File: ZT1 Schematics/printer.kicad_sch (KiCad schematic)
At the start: 5 parts, among them P103 Conn_02x20_Odd_Even, U101 74LS74, U102 74LS373, U103 74LS02

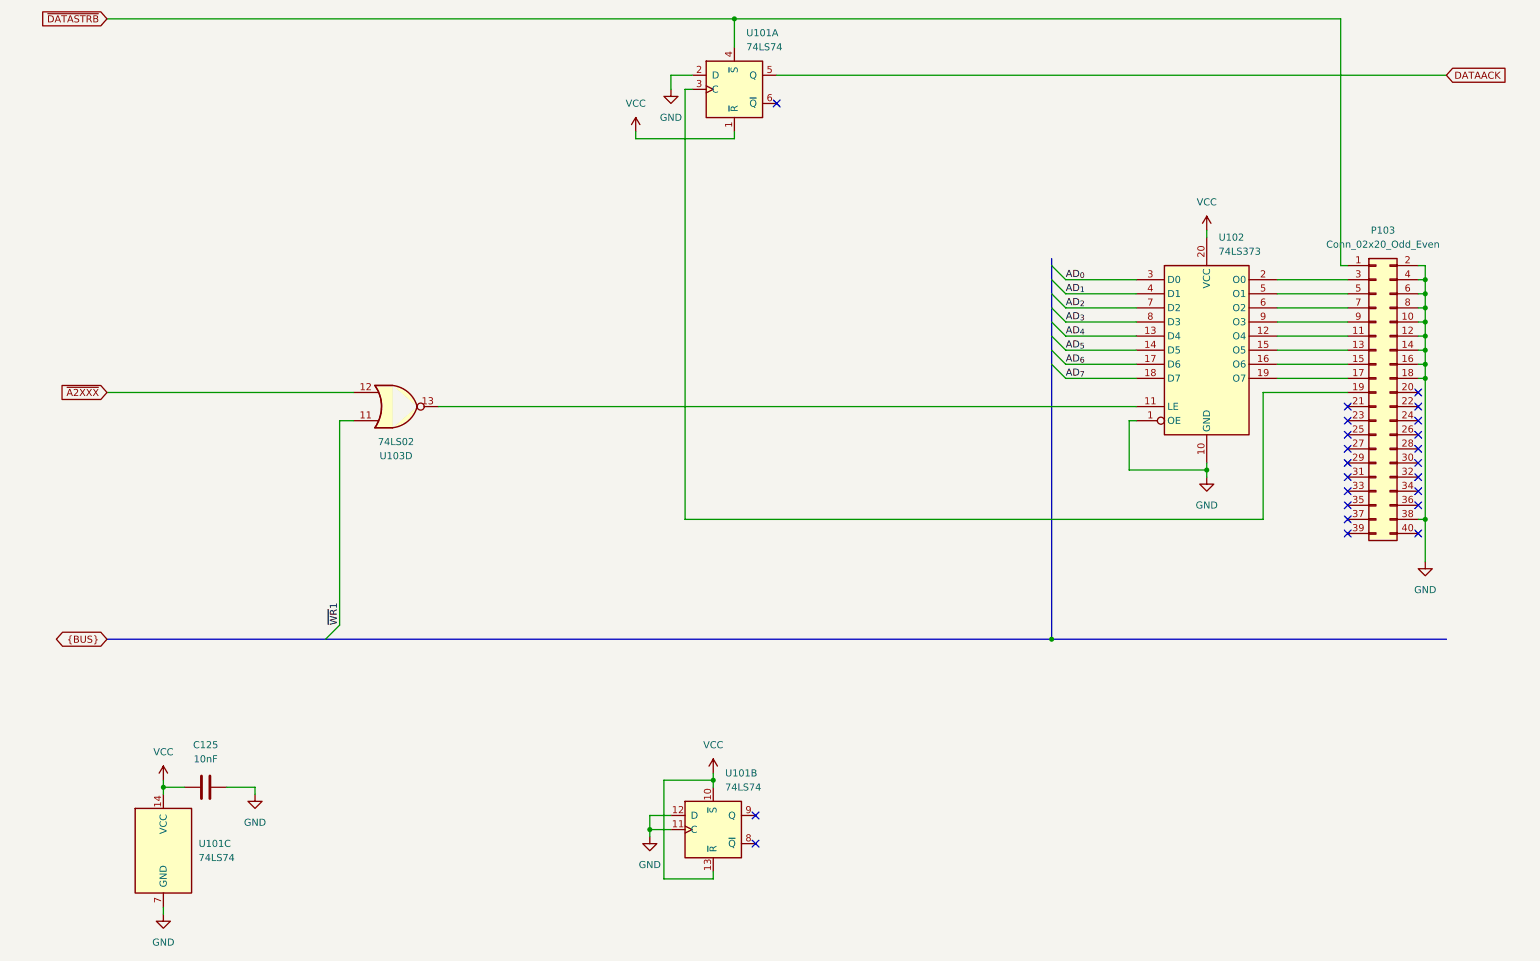
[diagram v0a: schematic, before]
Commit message: Minor touchups
Fixed some of the text
Added some explanations
Simplified the video circuit
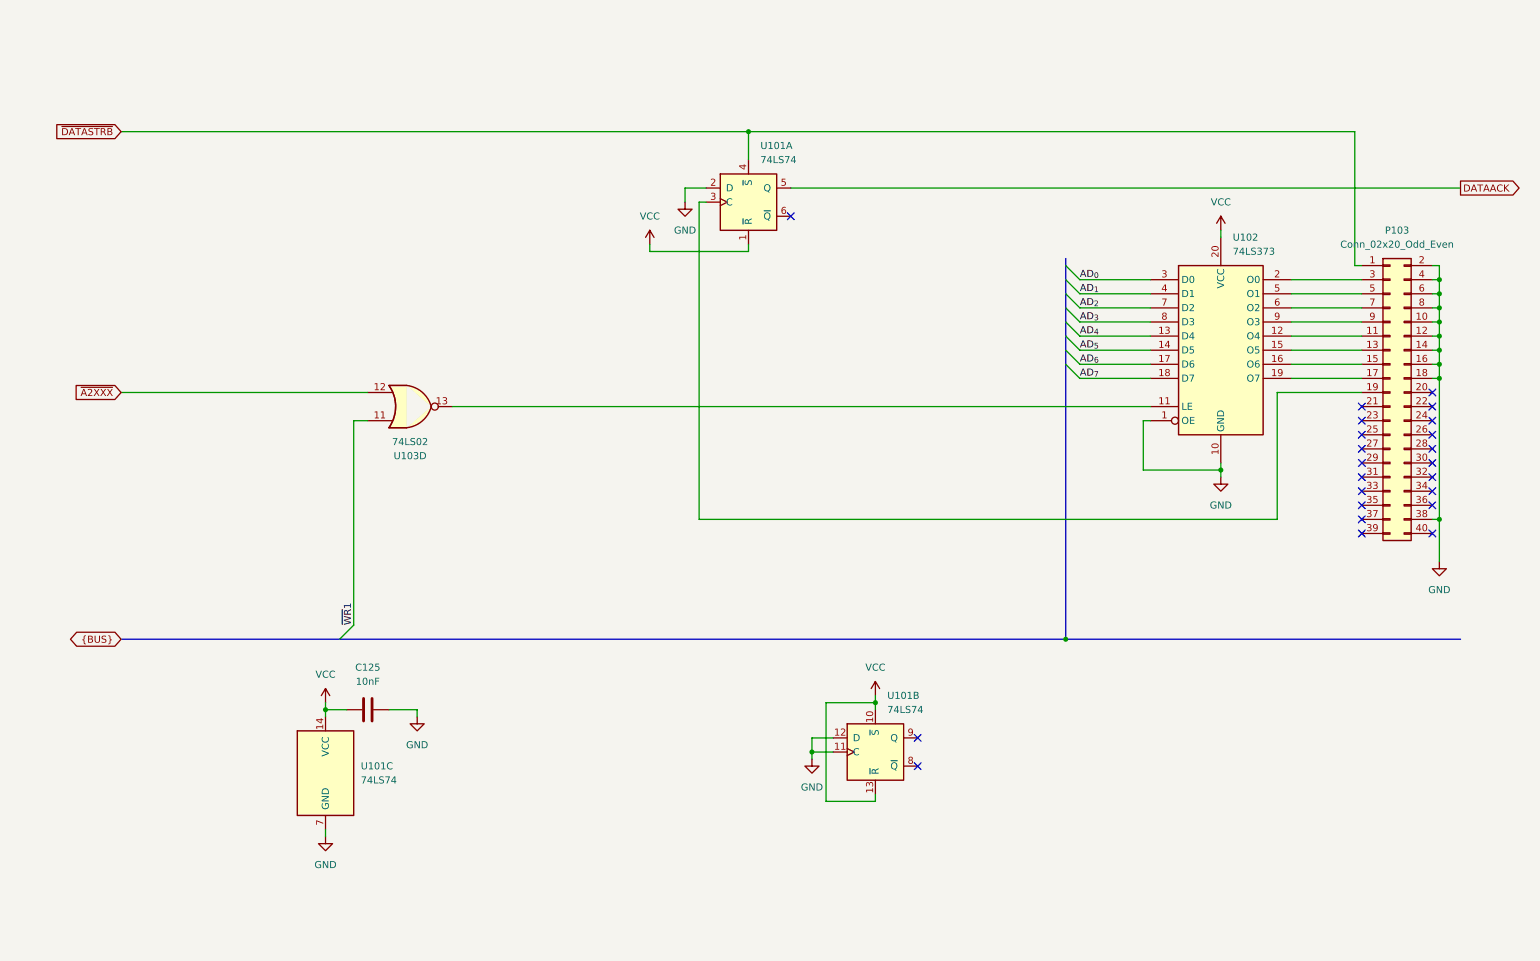
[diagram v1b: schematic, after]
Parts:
- C125: footprint ZX1:C_350mil -> ZT1:C_350mil
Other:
- moved on the sheet: C125, P103, U101A, U101B, U101C, U102, U103D
